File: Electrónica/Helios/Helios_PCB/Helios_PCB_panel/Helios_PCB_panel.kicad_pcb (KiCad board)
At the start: 2 copper layers, 160 x 160 mm, 51 parts, among them M0_0 Conn_01x04_Pin, M0_1 Conn_01x04_Pin, M0_2 Conn_01x04_Pin, M0_3 Conn_01x04_Pin, M1_0 Conn_01x04_Pin, M1_1 Conn_01x04_Pin, M1_2 Conn_01x04_Pin, M1_3 Conn_01x04_Pin, M2_0 Conn_01x04_Pin, M2_1 Conn_01x04_Pin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

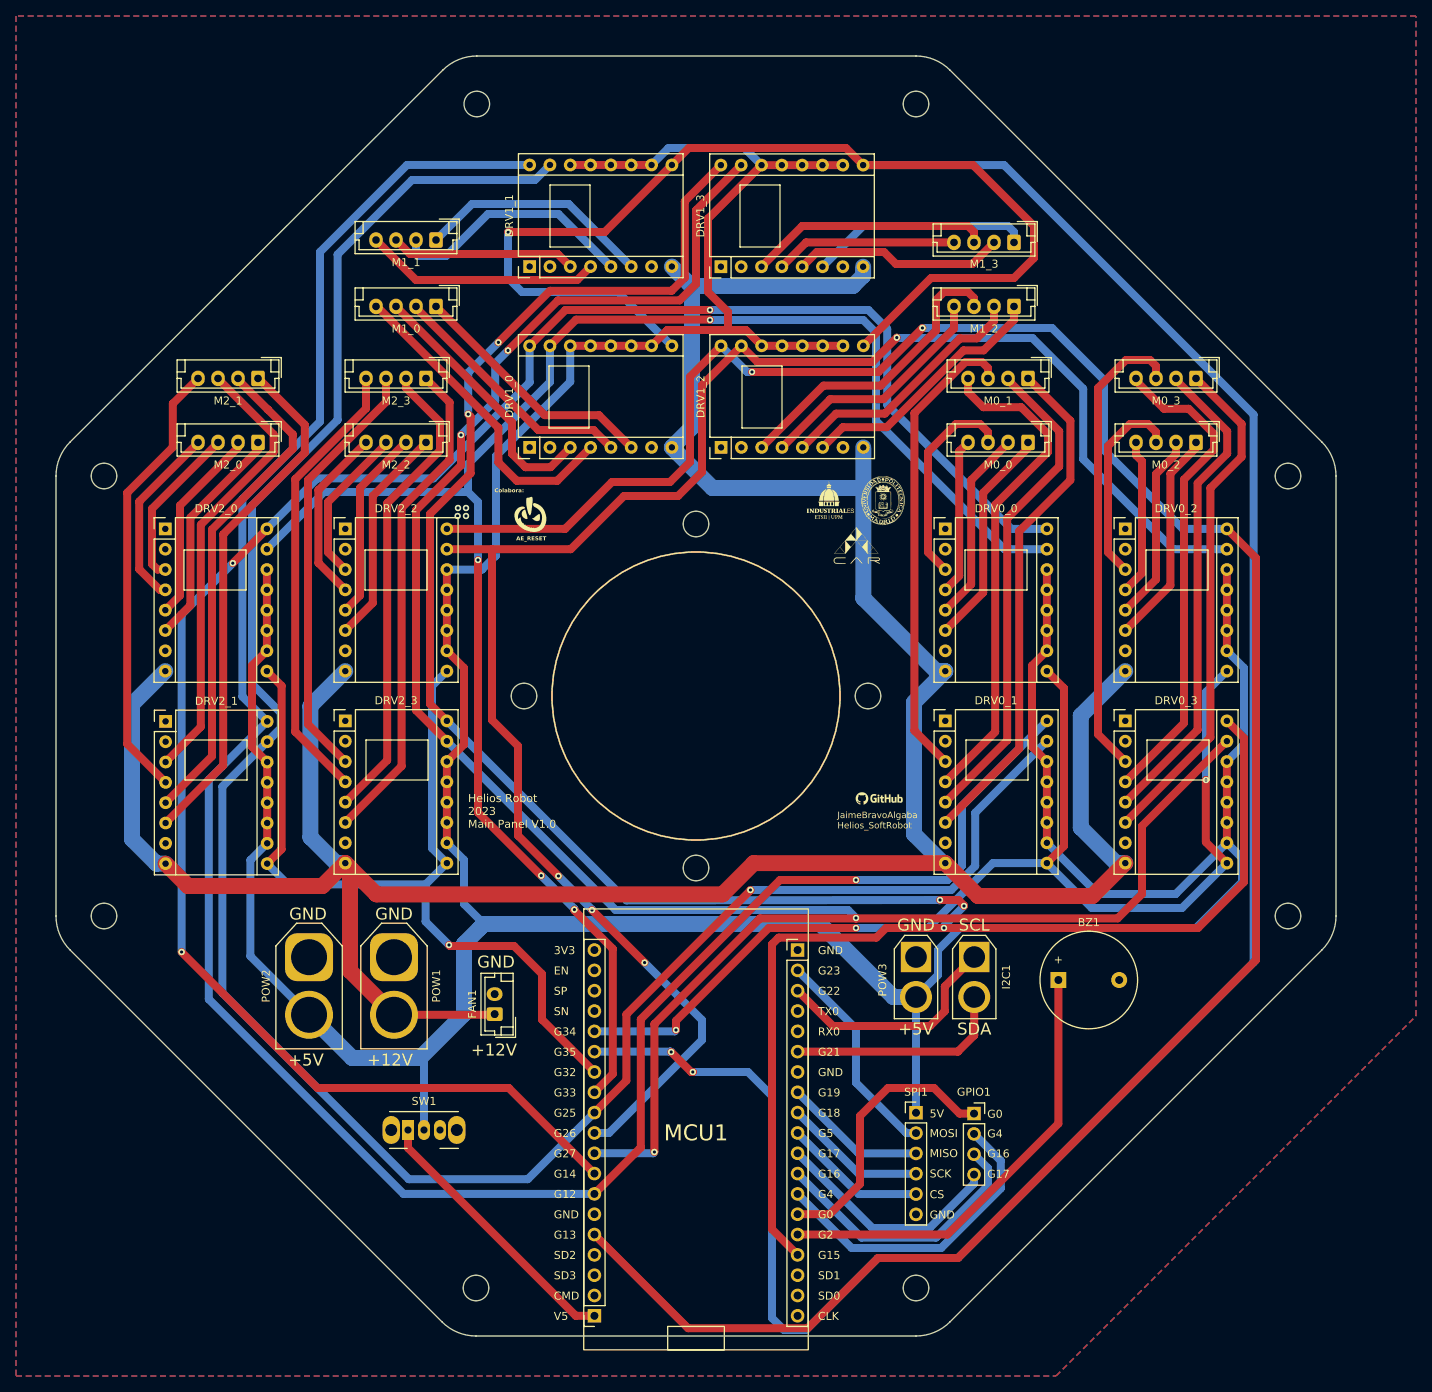
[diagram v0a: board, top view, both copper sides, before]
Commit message: Generated STL files for pulley actuator
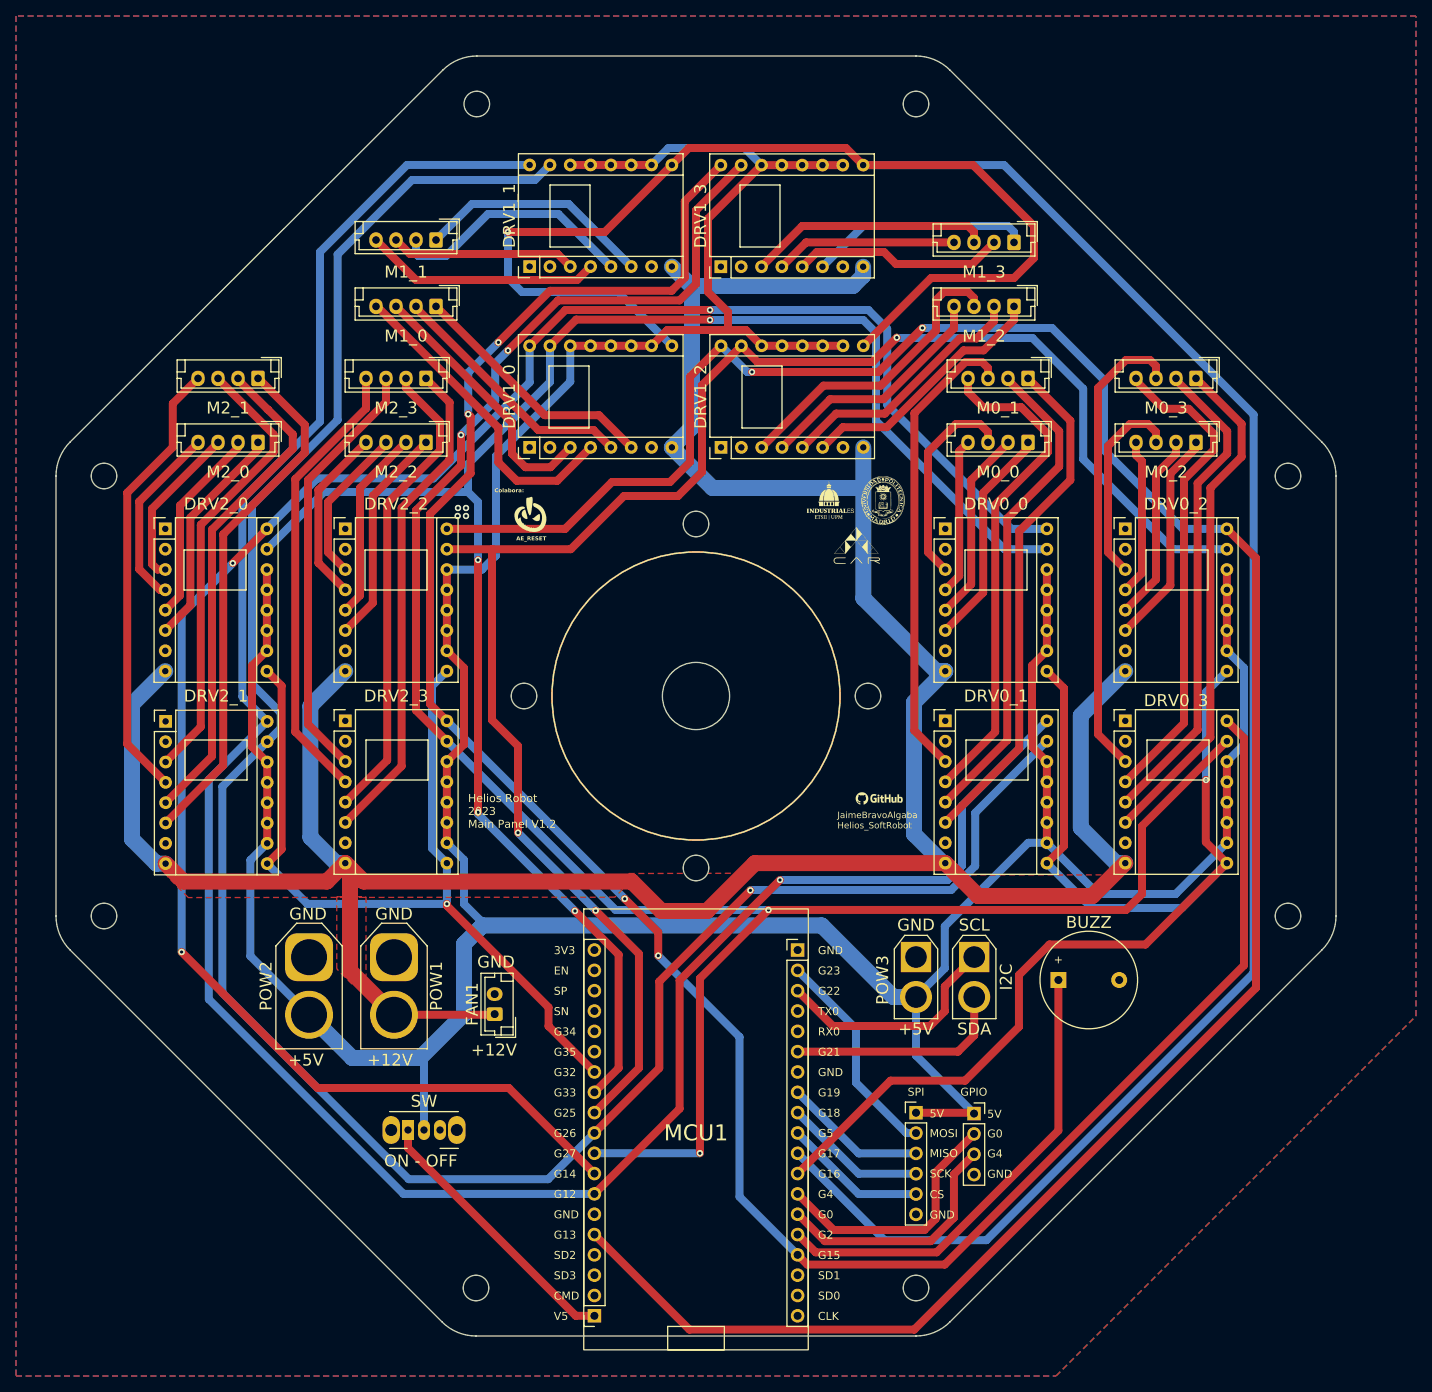
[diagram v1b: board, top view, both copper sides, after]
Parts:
- added H13: MountingHole, MountingHole:MountingHole_8.4mm_M8, F.Cu at (110.0, 100.0)
- renumbered BZ1 to BUZZ, GPIO1 to GPIO, I2C1 to I2C, SPI1 to SPI, SW1 to SW
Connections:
- GPIO pad 1: Net-(GPIO1-Pin_1) -> +5V
- GPIO pad 4: Net-(GPIO1-Pin_4) -> GND
- MCU1 pad 10: S2 -> S1
- MCU1 pad 25: Net-(GPIO1-Pin_1) -> Net-(GPIO1-Pin_3)
- MCU1 pad 27: Net-(GPIO1-Pin_3) -> EN0
- MCU1 pad 28: Net-(GPIO1-Pin_4) -> EN1
- MCU1 pad 5: EN0 -> unconnected-(MCU1-G34-Pad5)
- MCU1 pad 6: EN1 -> unconnected-(MCU1-G35-Pad6)
- MCU1 pad 9: S1 -> S2
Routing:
- net EN1: track 396.3 -> 340.6 mm, vias 3 -> 1
- net Net-(GPIO1-Pin_1): track 34.9 -> 0.00 mm
- net Net-(GPIO1-Pin_4): track 29.4 -> 0.00 mm
- net +5V: track 513.6 -> 497.1 mm
- net D3: track 296.1 -> 282.7 mm, vias 5 -> 4
- net S2: track 223.1 -> 212.9 mm, vias 4 -> 3
- net S3: track 274.4 -> 266.4 mm
- net EN0: track 145.0 -> 152.6 mm, vias 3 -> 1
- net Net-(GPIO1-Pin_2): track 39.5 -> 32.3 mm
- net Net-(GPIO1-Pin_3): track 34.5 -> 31.1 mm
- net EN2: track 112.6 -> 109.4 mm
- net BUZZ: track 56.3 -> 58.7 mm
- net D2: track 294.4 -> 296.6 mm
- net S1: track 276.6 -> 278.0 mm
- net +12V: track 383.1 -> 384.4 mm
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- added copper zone on F.Cu, net +12V
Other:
- board text added: "Helios Robot 2023 Main Panel V1.2"
- board text added: "ON - OFF"
- board text removed: "G16"
- board text removed: "G17"
- board text removed: "Helios Robot 2023 Main Panel V1.0"

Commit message: Update
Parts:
- removed H13: MountingHole, MountingHole:MountingHole_8.4mm_M8
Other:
- outline, holes or cut-outs redrawn
